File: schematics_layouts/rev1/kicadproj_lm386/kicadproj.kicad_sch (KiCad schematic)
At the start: 49 parts, among them Q1 Si2323DS, Q2 Si2323DS, SW1 WAKE Switch, SW2 SET 15MIN, SW3 LOUD, SW4 NIGHT, U2 ATmega328P-PU

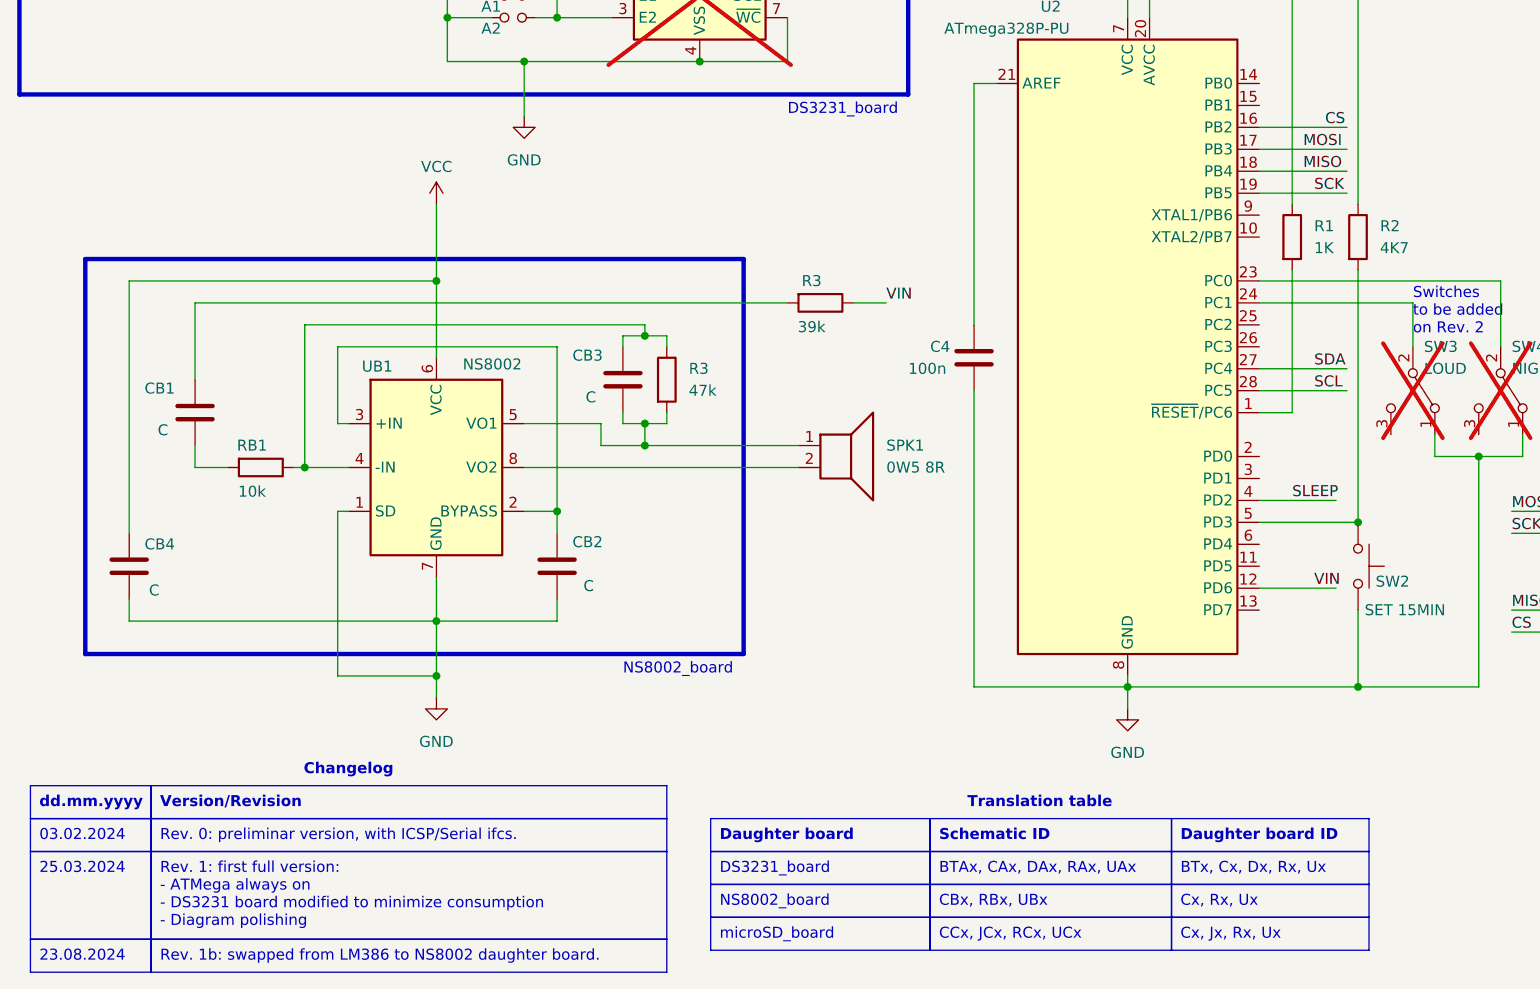
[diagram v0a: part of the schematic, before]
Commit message: Updated schematic for NS8002 (Schematic revision 1b); Updated wiki page and figures
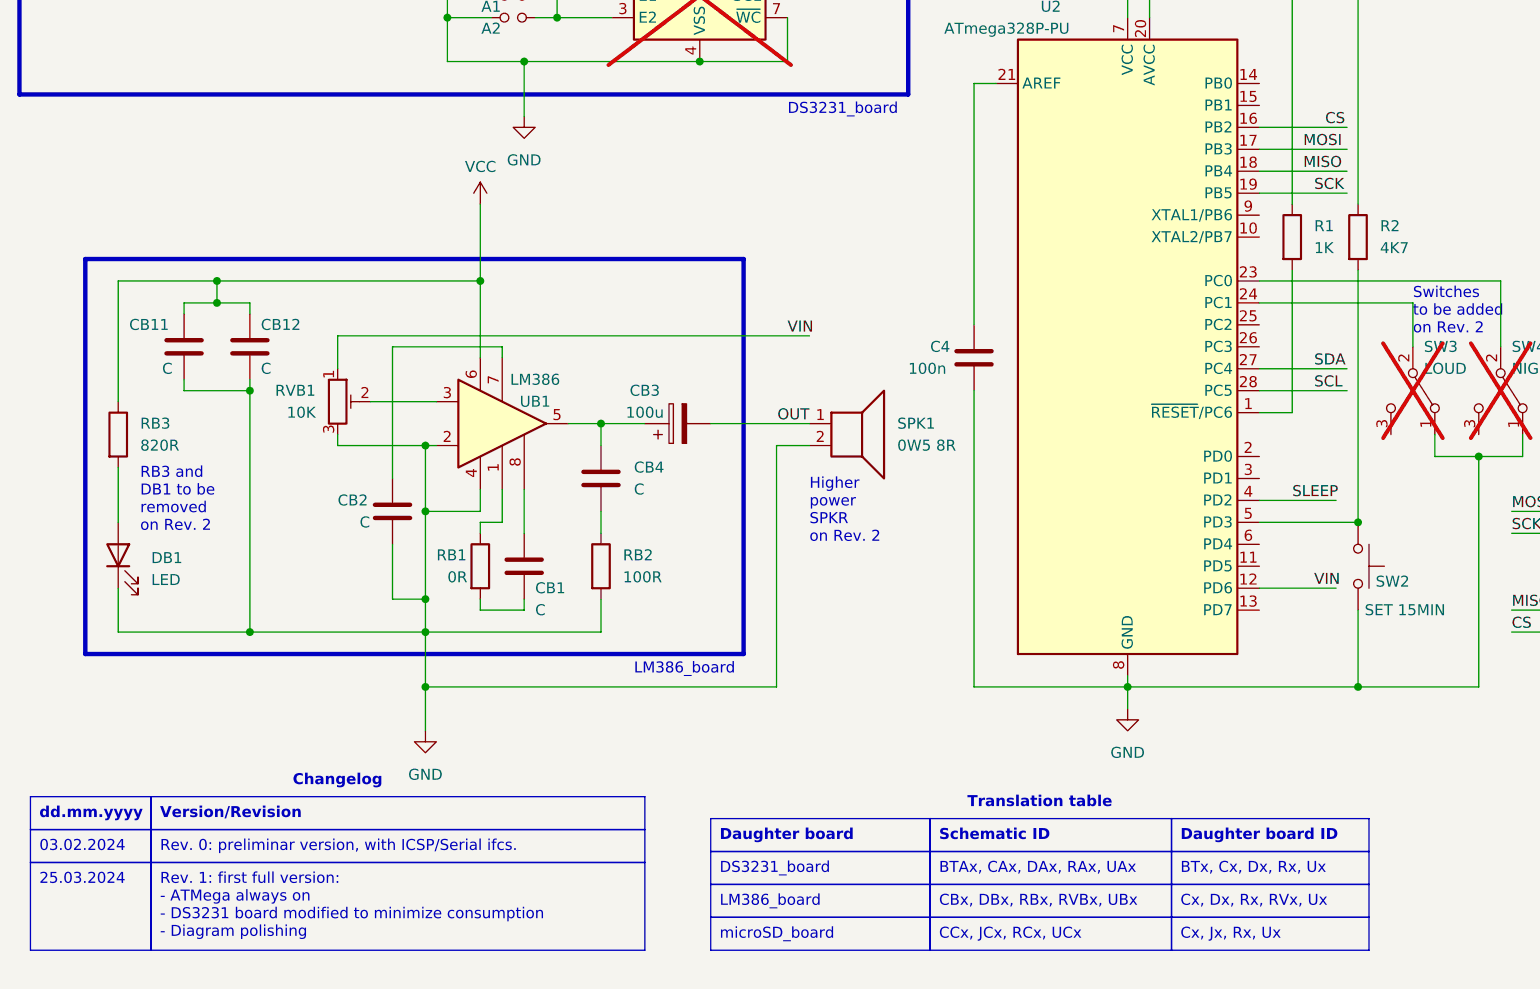
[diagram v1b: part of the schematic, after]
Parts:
- removed CB3: C, symbol Device:C
- removed R3: 39k, symbol Device:R
- removed R3: 47k, symbol Device:R
- removed UB1: NS8002, Package_SO:TSSOP-8_3x3mm_P0.65mm, symbol Amplifier_Audio:LM4810
- added CB11, CB12: C, symbol Device:C
- added CB3: 100u, symbol Device:CP
- added DB1: LED, symbol Device:LED
- added RB2: 100R, symbol Device:R
- added RB3: 820R, symbol Device:R
- added RVB1: 10K, symbol Device:R_POT_TRIM
- added UB1: LM386, symbol Amplifier_Audio:LM386
- RB1: value 10k -> 0R
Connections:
- net GND: now also SPK1.2, CB11.2, CB12.2, DB1.1 (K), RB2.2, RVB1.3, UB1.2 (-), UB1.4 (GND); no longer CB4.2
- net VCC: now also CB11.1, CB12.1, RB3.1, UB1.6 (V+); no longer CB4.1
- net VIN: now also RVB1.1
- net at CB2.1: now also UB1.7 (BYPASS)
- net at CB1.1: now also UB1.8 (GAIN)
- net OUT: now reaches SPK1.1
- net OUT: now also CB3.2
- net at RB1.1: now also UB1.1 (GAIN)
- new net: RVB1.2, UB1.3 (+)
- new net: CB3.1, CB4.1, UB1.5
- new net: CB4.2, RB2.1
- new net: DB1.2 (A), RB3.2
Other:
- note added: "Higher power SPKR on Rev. 2"
- note added: "LM386_board"
- note added: "RB3 and DB1 to be removed on Rev. 2"
- note removed: "NS8002_board"
- moved on the sheet: SPK1
